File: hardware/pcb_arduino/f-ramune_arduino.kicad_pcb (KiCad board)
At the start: 2 copper layers, 73.7 x 55.9 mm, 15 parts, among them Q1 IRL520N, SW1 SW_Push, U1 74HC595, U2 74HC595, U3 Memory (Socket)

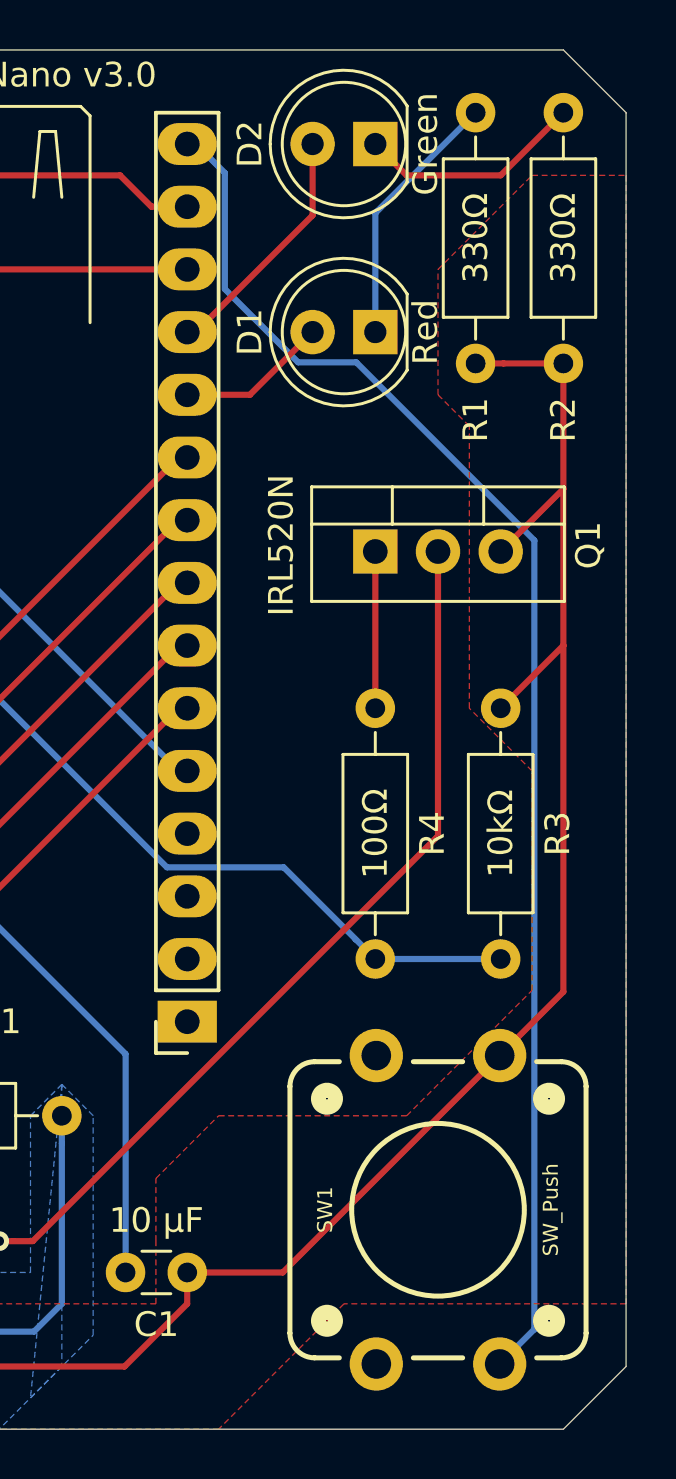
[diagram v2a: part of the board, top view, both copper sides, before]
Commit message: The pin assignments on this switch footprint are wrong. The switch does not close between the long side of the part's pins - it closes around the short side.
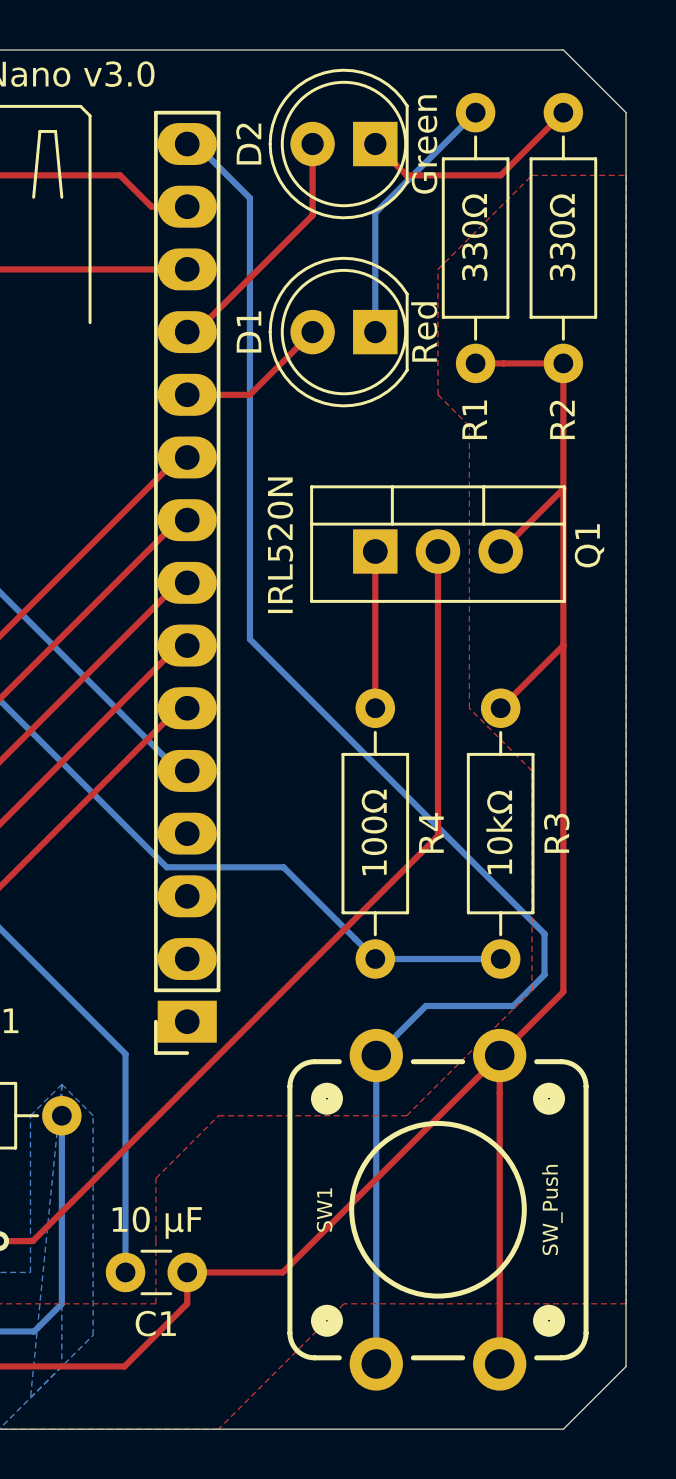
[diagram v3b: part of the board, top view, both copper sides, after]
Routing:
- net GND: track 213.6 -> 226.1 mm
- net Net-(A1-Pad15): track 57.4 -> 60.5 mm
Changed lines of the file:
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@@
     (thickness 1.6)
     (drawings 27)
-    (tracks 407)
+    (tracks 410)
     (zones 0)
     (modules 15)
@@
     (add_net ~OE)
     (add_net ~WE)
+  )
+  (module f-ramune:TACTILE_SWITCH_PTH_12MM (layer F.Cu)
+    (at 182.88 121.92 90)
+    (descr "MOMENTARY SWITCH (PUSHBUTTON) - SPST - PTH, 12MM SQUARE")
+    (tags "MOMENTARY SWITCH (PUSHBUTTON) - SPST - PTH, 12MM SQUARE")
+    (attr virtual)
+    (fp_text reference SW1 (at 0 -4.572 90) (layer F.SilkS)
+      (effects (font (size 0.6096 0.6096) (thickness 0.127)))
+    )
+    (fp_text value SW_Push (at 0 4.572 90) (layer F.SilkS)
+      (effects (font (size 0.6096 0.6096) (thickness 0.127)))
+    )
+    (fp_arc (start -4.99872 4.99872) (end -4.99872 5.99948) (angle 90) (layer F.SilkS) (width 0.2032))
+    (fp_arc (start 4.99872 4.99872) (end 5.99948 4.99872) (angle 90) (layer F.SilkS) (width 0.2032))
+    (fp_arc (start 4.99872 -4.99872) (end 4.99872 -5.99948) (angle 90) (layer F.SilkS) (width 0.2032))
+    (fp_arc (start -4.99872 -4.99872) (end -5.99948 -4.99872) (angle 90) (layer F.SilkS) (width 0.2032))
+    (fp_circle (center -4.49834 4.49834) (end -4.49834 4.19862) (layer F.SilkS) (width 0.6985))
+    (fp_circle (center 4.49834 4.49834) (end 4.49834 4.19862) (layer F.SilkS) (width 0.6985))
+    (fp_circle (center 4.49834 -4.49834) (end 4.49834 -4.79806) (layer F.SilkS) (width 0.6985))
+    (fp_circle (center -4.49834 -4.49834) (end -4.49834 -4.79806) (layer F.SilkS) (width 0.6985))
+    (fp_circle (center 0 0) (end 0 -3.49758) (layer F.SilkS) (width 0.2032))
+    (fp_line (start -5.99948 0.99822) (end -5.99948 -0.99822) (layer F.SilkS) (width 0.2032))
+    (fp_line (start -5.99948 4.99872) (end -5.99948 3.99796) (layer F.SilkS) (width 0.2032))
+    (fp_line (start 4.99872 5.99948) (end -4.99872 5.99948) (layer F.SilkS) (width 0.2032))
+    (fp_line (start 5.99948 3.99796) (end 5.99948 4.99872) (layer F.SilkS) (width 0.2032))
+    (fp_line (start 5.99948 -0.99822) (end 5.99948 0.99822) (layer F.SilkS) (width 0.2032))
+    (fp_line (start 5.99948 -4.99872) (end 5.99948 -3.99796) (layer F.SilkS) (width 0.2032))
+    (fp_line (start -4.99872 -5.99948) (end 4.99872 -5.99948) (layer F.SilkS) (width 0.2032))
+    (fp_line (start -5.99948 -3.99796) (end -5.99948 -4.99872) (layer F.SilkS) (width 0.2032))
+    (fp_line (start 4.99872 -0.19812) (end 4.99872 -0.99822) (layer Dwgs.User) (width 0.2032))
+    (fp_line (start 4.99872 0.6985) (end 4.49834 0.19812) (layer Dwgs.User) (width 0.2032))
+    (fp_line (start 4.99872 1.29794) (end 4.99872 0.6985) (layer Dwgs.User) (width 0.2032))
+    (pad 2 thru_hole circle (at -6.2484 -2.49936 90) (size 2.159 2.159) (drill 1.19888) (layers *.Cu *.Mask)
+      (net 2 "Net-(A1-Pad15)") (solder_mask_margin 0.1016))
+    (pad 2 thru_hole circle (at 6.2484 -2.49936 90) (size 2.159 2.159) (drill 1.19888) (layers *.Cu *.Mask)
+      (net 2 "Net-(A1-Pad15)") (solder_mask_margin 0.1016))
+    (pad 1 thru_hole circle (at -6.2484 2.49936 90) (size 2.159 2.159) (drill 1.19888) (layers *.Cu *.Mask)
+      (net 5 GND) (solder_mask_margin 0.1016))
+    (pad 1 thru_hole circle (at 6.2484 2.49936 90) (size 2.159 2.159) (drill 1.19888) (layers *.Cu *.Mask)
+      (net 5 GND) (solder_mask_margin 0.1016))
   )
   (module f-ramune:Logo_OpenSourceHW (layer B.Cu)
@@
     )
   )
-  (module f-ramune:TACTILE_SWITCH_PTH_12MM (layer F.Cu)
-    (at 182.88 121.92 90)
-    (descr "MOMENTARY SWITCH (PUSHBUTTON) - SPST - PTH, 12MM SQUARE")
-    (tags "MOMENTARY SWITCH (PUSHBUTTON) - SPST - PTH, 12MM SQUARE")
-    (attr virtual)
-    (fp_text reference SW1 (at 0 -4.572 90) (layer F.SilkS)
-      (effects (font (size 0.6096 0.6096) (thickness 0.127)))
-    )
-    (fp_text value SW_Push (at 0 4.572 90) (layer F.SilkS)
-      (effects (font (size 0.6096 0.6096) (thickness 0.127)))
-    )
-    (fp_arc (start -4.99872 4.99872) (end -4.99872 5.99948) (angle 90) (layer F.SilkS) (width 0.2032))
-    (fp_arc (start 4.99872 4.99872) (end 5.99948 4.99872) (angle 90) (layer F.SilkS) (width 0.2032))
-    (fp_arc (start 4.99872 -4.99872) (end 4.99872 -5.99948) (angle 90) (layer F.SilkS) (width 0.2032))
-    (fp_arc (start -4.99872 -4.99872) (end -5.99948 -4.99872) (angle 90) (layer F.SilkS) (width 0.2032))
-    (fp_circle (center -4.49834 4.49834) (end -4.49834 4.19862) (layer F.SilkS) (width 0.6985))
-    (fp_circle (center 4.49834 4.49834) (end 4.49834 4.19862) (layer F.SilkS) (width 0.6985))
-    (fp_circle (center 4.49834 -4.49834) (end 4.49834 -4.79806) (layer F.SilkS) (width 0.6985))
-    (fp_circle (center -4.49834 -4.49834) (end -4.49834 -4.79806) (layer F.SilkS) (width 0.6985))
-    (fp_circle (center 0 0) (end 0 -3.49758) (layer F.SilkS) (width 0.2032))
-    (fp_line (start -5.99948 0.99822) (end -5.99948 -0.99822) (layer F.SilkS) (width 0.2032))
-    (fp_line (start -5.99948 4.99872) (end -5.99948 3.99796) (layer F.SilkS) (width 0.2032))
-    (fp_line (start 4.99872 5.99948) (end -4.99872 5.99948) (layer F.SilkS) (width 0.2032))
-    (fp_line (start 5.99948 3.99796) (end 5.99948 4.99872) (layer F.SilkS) (width 0.2032))
-    (fp_line (start 5.99948 -0.99822) (end 5.99948 0.99822) (layer F.SilkS) (width 0.2032))
-    (fp_line (start 5.99948 -4.99872) (end 5.99948 -3.99796) (layer F.SilkS) (width 0.2032))
-    (fp_line (start -4.99872 -5.99948) (end 4.99872 -5.99948) (layer F.SilkS) (width 0.2032))
-    (fp_line (start -5.99948 -3.99796) (end -5.99948 -4.99872) (layer F.SilkS) (width 0.2032))
-    (fp_line (start 4.99872 -0.19812) (end 4.99872 -0.99822) (layer Dwgs.User) (width 0.2032))
-    (fp_line (start 4.99872 0.6985) (end 4.49834 0.19812) (layer Dwgs.User) (width 0.2032))
-    (fp_line (start 4.99872 1.29794) (end 4.99872 0.6985) (layer Dwgs.User) (width 0.2032))
-    (pad 4 thru_hole circle (at -6.2484 -2.49936 90) (size 2.159 2.159) (drill 1.19888) (layers *.Cu *.Mask)
-      (solder_mask_margin 0.1016))
-    (pad 3 thru_hole circle (at 6.2484 -2.49936 90) (size 2.159 2.159) (drill 1.19888) (layers *.Cu *.Mask)
-      (solder_mask_margin 0.1016))
-    (pad 2 thru_hole circle (at -6.2484 2.49936 90) (size 2.159 2.159) (drill 1.19888) (layers *.Cu *.Mask)
-      (net 2 "Net-(A1-Pad15)") (solder_mask_margin 0.1016))
-    (pad 1 thru_hole circle (at 6.2484 2.49936 90) (size 2.159 2.159) (drill 1.19888) (layers *.Cu *.Mask)
-      (net 5 GND) (solder_mask_margin 0.1016))
-  )
   (module f-ramune:R_Axial_DIN0207_L6.3mm_D2.5mm_P10.16mm_Horizontal (layer F.Cu)
     (at 167.64 118.11 180)
@@
   (segment (start 121.05 83.82) (end 125.00499 79.86501) (width 0.25) (layer F.Cu) (net 1))
   (segment (start 120.65 83.82) (end 121.05 83.82) (width 0.25) (layer F.Cu) (net 1))
+  (segment (start 180.38064 128.1684) (end 180.38064 115.6716) (width 0.25) (layer B.Cu) (net 2))
   (segment (start 173.07 78.74) (end 172.72 78.74) (width 0.25) (layer B.Cu) (net 2))
-  (segment (start 174.24501 79.91501) (end 173.07 78.74) (width 0.25) (layer B.Cu) (net 2))
-  (segment (start 177.211999 87.585001) (end 174.24501 84.618012) (width 0.25) (layer B.Cu) (net 2))
-  (segment (start 179.568003 87.585001) (end 177.211999 87.585001) (width 0.25) (layer B.Cu) (net 2))
-  (segment (start 186.783861 94.800859) (end 179.568003 87.585001) (width 0.25) (layer B.Cu) (net 2))
-  (segment (start 174.24501 84.618012) (end 174.24501 79.91501) (width 0.25) (layer B.Cu) (net 2))
-  (segment (start 186.783861 126.763899) (end 186.783861 94.800859) (width 0.25) (layer B.Cu) (net 2))
-  (segment (start 185.37936 128.1684) (end 186.783861 126.763899) (width 0.25) (layer B.Cu) (net 2))
+  (segment (start 175.26 80.93) (end 173.07 78.74) (width 0.25) (layer B.Cu) (net 2))
+  (segment (start 182.38724 113.665) (end 185.928 113.665) (width 0.25) (layer B.Cu) (net 2))
+  (segment (start 180.38064 115.6716) (end 182.38724 113.665) (width 0.25) (layer B.Cu) (net 2))
+  (segment (start 185.928 113.665) (end 187.198 112.395) (width 0.25) (layer B.Cu) (net 2))
+  (segment (start 187.198 112.395) (end 187.198 110.744) (width 0.25) (layer B.Cu) (net 2))
+  (segment (start 187.198 110.744) (end 175.26 98.806) (width 0.25) (layer B.Cu) (net 2))
+  (segment (start 175.26 98.806) (end 175.26 80.93) (width 0.25) (layer B.Cu) (net 2))
   (segment (start 155.39641 80.01) (end 154.12641 81.28) (width 0.25) (layer F.Cu) (net 4))
   (segment (start 170 80.01) (end 155.39641 80.01) (width 0.25) (layer F.Cu) (net 4))
@@
   (segment (start 185.53537 87.63) (end 187.96 87.63) (width 0.25) (layer F.Cu) (net 5))
   (segment (start 184.404 87.63) (end 185.53537 87.63) (width 0.25) (layer F.Cu) (net 5))
+  (segment (start 185.37936 117.198243) (end 185.37936 128.1684) (width 0.25) (layer F.Cu) (net 5))
+  (segment (start 185.37936 115.6716) (end 185.37936 117.198243) (width 0.25) (layer F.Cu) (net 5))
   (segment (start 162.031715 83.82) (end 160.761715 82.55) (width 0.25) (layer F.Cu) (net 6))
   (segment (start 172.72 83.82) (end 162.031715 83.82) (width 0.25) (layer F.Cu) (net 6))

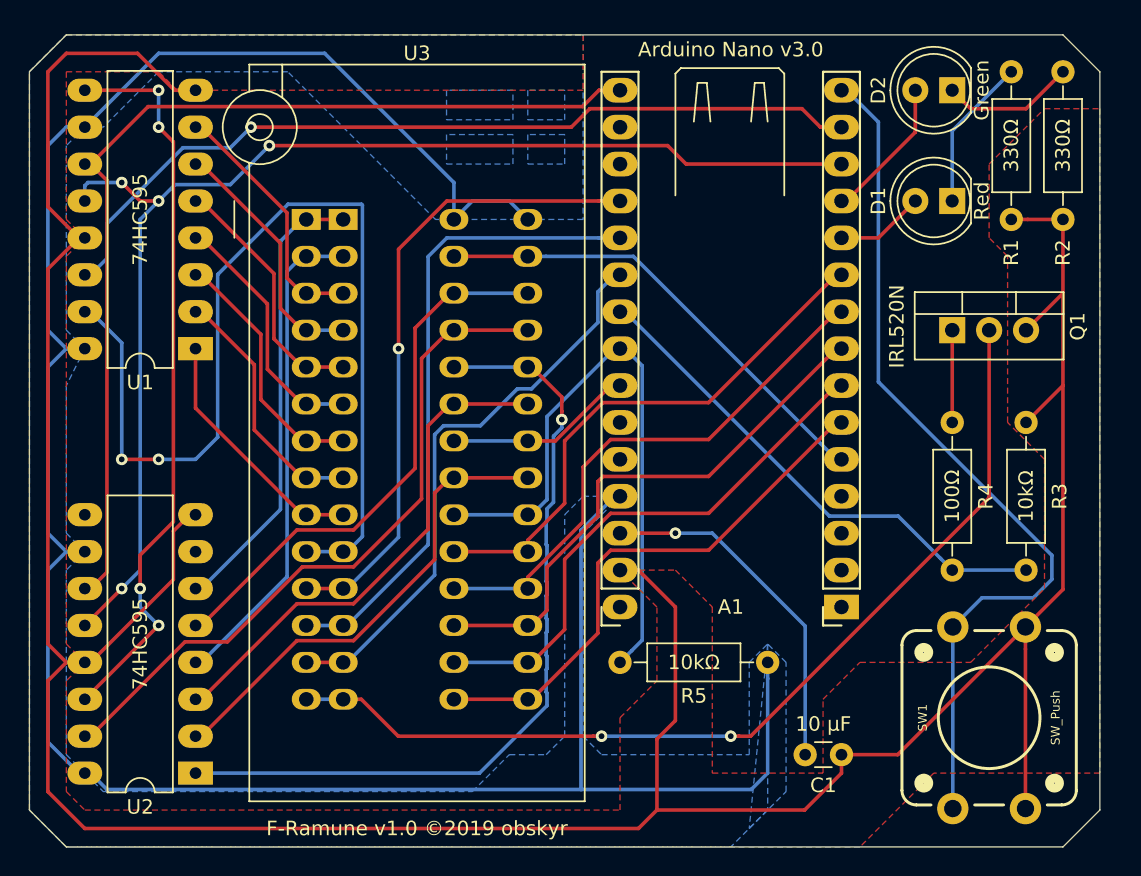
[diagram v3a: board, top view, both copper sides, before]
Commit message: Update / tidy up the Arduino version and add the instructions on the back
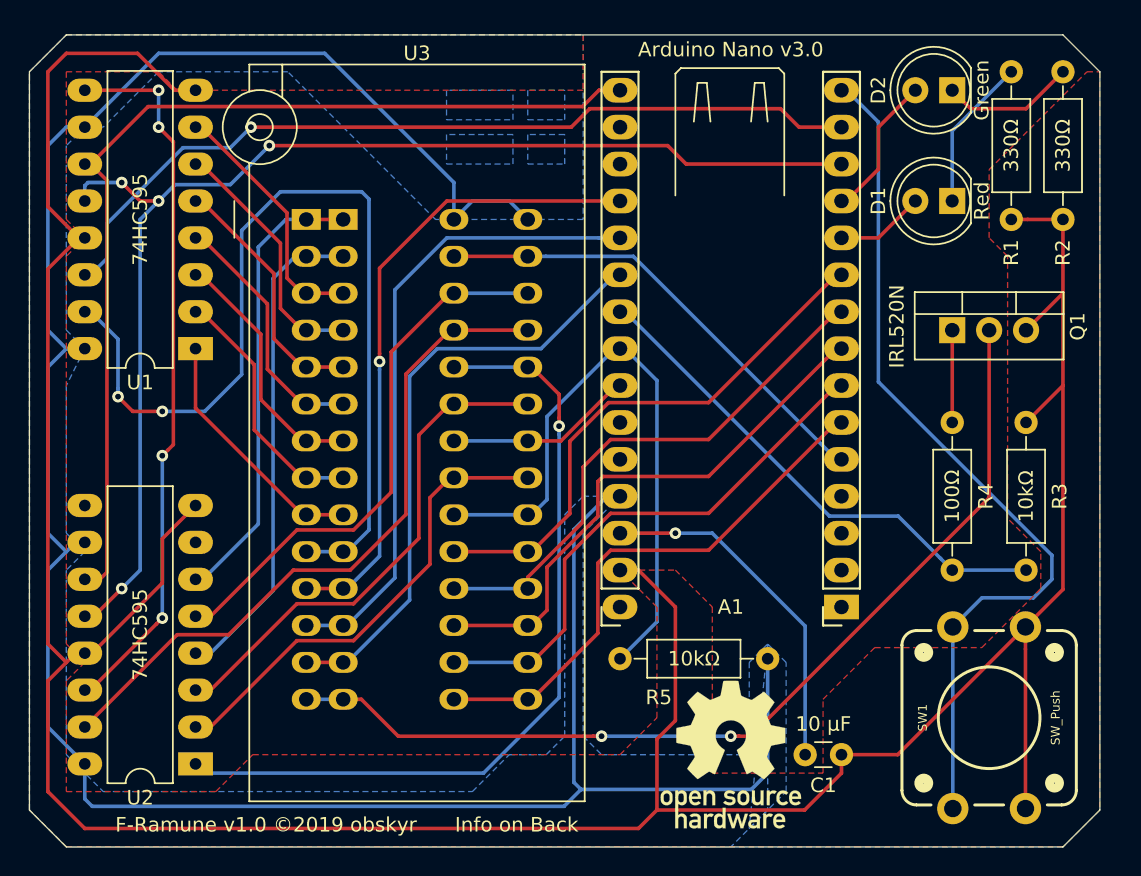
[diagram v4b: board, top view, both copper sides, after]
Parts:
- G***: moved to F.Cu
- moved U2 0.64 mm to (128.3, 125.1)
- moved R5 0.25 mm to (167.6, 117.9)
- turned G*** to 0 degrees
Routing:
- net A0: track 69.0 -> 64.7 mm
- net +5V: track 169.1 -> 172.1 mm
- net D2: track 39.5 -> 41.7 mm
- net Net-(U1-Pad9): track 51.4 -> 49.9 mm
- net ~CE: track 42.6 -> 43.2 mm
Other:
- board text added: "F-Ramune v1.0 ©2019 obskyr Info on Back"
- board text added: "F-Ramune v1.0 ©2019 obskyr https://github.com/obskyr/f-ramune/"
- board text added: "Insert chip into socket. Press button to test. GREEN: FRAM is genuine. RED: FRAM is counterfeit. GREEN+RED: FRAM is faulty."
- board text removed: "F-Ramune v1.0 ©2019 obskyr"
- board text removed: "https://github.com/obskyr/f-ramune/"
